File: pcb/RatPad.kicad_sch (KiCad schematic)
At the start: 26 parts, among them SW1 SW_Push, SW2 SW_Push, SW3 SW_Push, SW4 SW_Push, SW5 SW_Push, SW6 SW_Push, SW7 SW_Push, SW8 SW_Push, U1 XIAO-RP2040-DIP

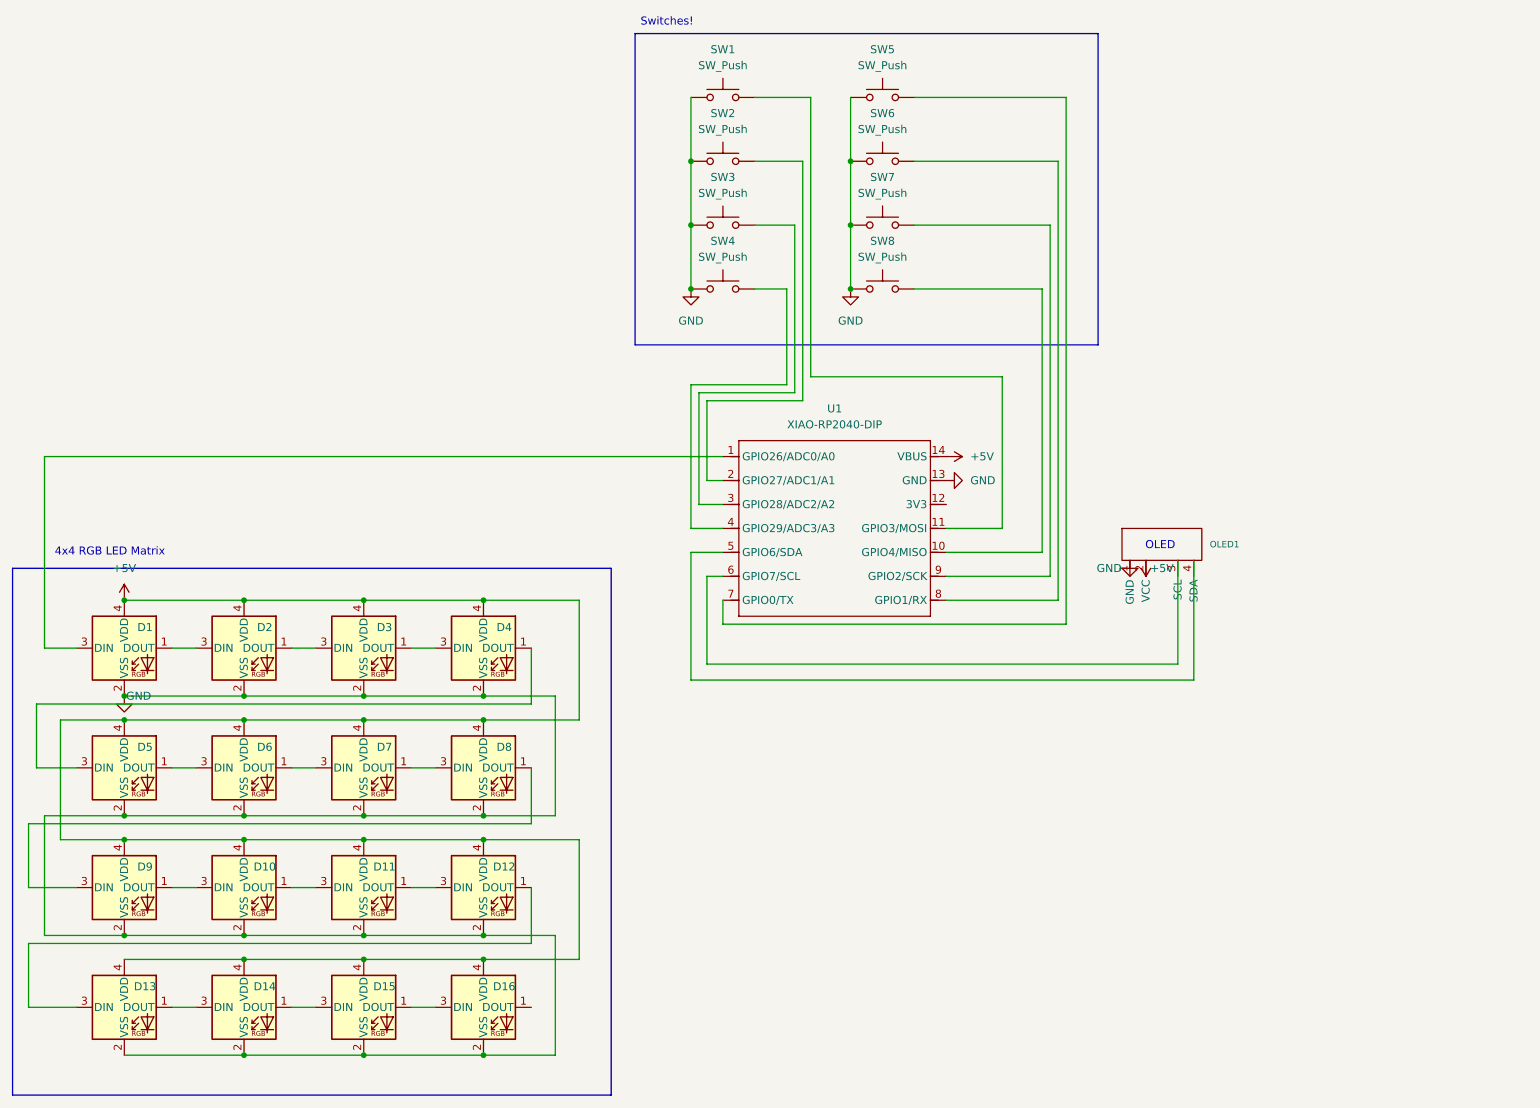
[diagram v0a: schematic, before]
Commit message: Add case and update PCB
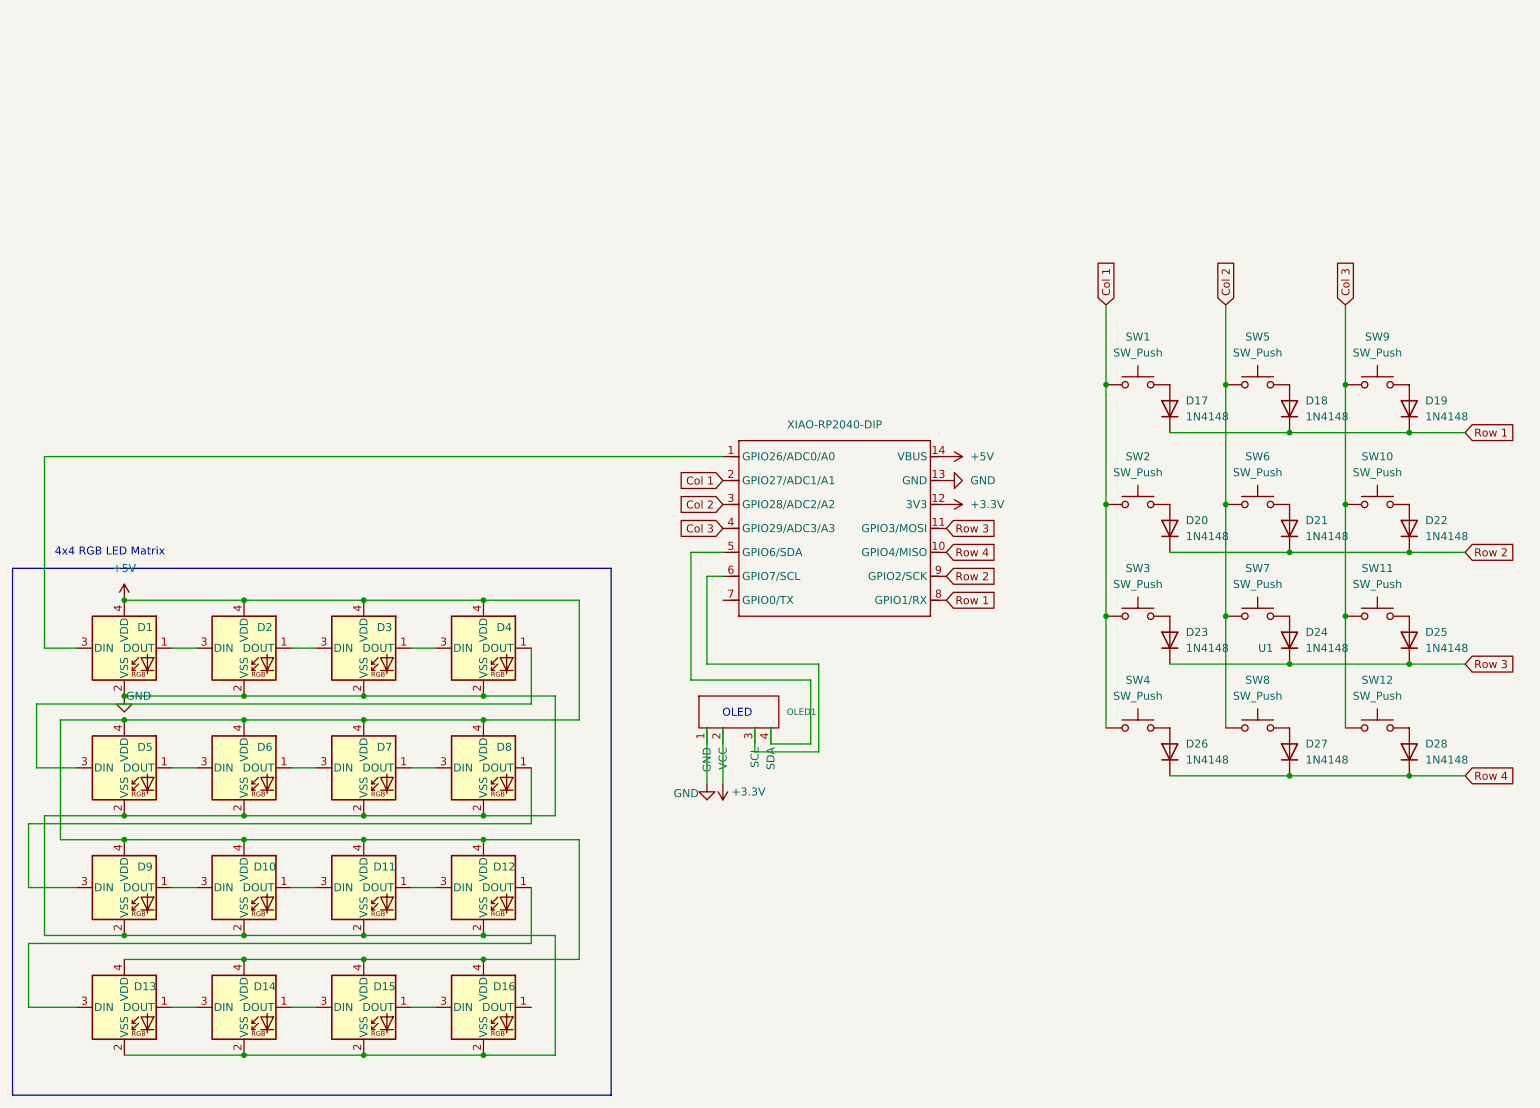
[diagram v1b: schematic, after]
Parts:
- added D17, D18, D19, D20, D21, D22, D23, D24, D25, D26, D27, D28: 1N4148, Diode_THT:D_DO-35_SOD27_P7.62mm_Horizontal, symbol Diode:1N4148
- added SW10, SW11, SW12, SW9: SW_Push, Button_Switch_Keyboard:SW_Cherry_MX_1.00u_PCB, symbol Switch:SW_Push
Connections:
- net +5V: no longer OLED1.2 (VCC)
- net GND: no longer SW1.1, SW2.1, SW3.1, SW4.1, SW5.1, SW6.1, SW7.1, SW8.1
- net at SW4.2: now also D26.2 (A); no longer U1.4 (GPIO29/ADC3/A3)
- net at SW5.2: now also D18.2 (A); no longer U1.7 (GPIO0/TX)
- net at SW7.2: now also D24.2 (A); no longer U1.9 (GPIO2/SCK)
- net at SW8.2: now also D27.2 (A); no longer U1.10 (GPIO4/MISO)
- net at SW1.2: now also D17.2 (A); no longer U1.11 (GPIO3/MOSI)
- net +3.3V: now reaches U1.12 (3V3)
- net +3.3V: now also OLED1.2 (VCC)
- net at SW2.2: now also D20.2 (A); no longer U1.2 (GPIO27/ADC1/A1)
- net at SW3.2: now also D23.2 (A); no longer U1.3 (GPIO28/ADC2/A2)
- net at SW6.2: now also D21.2 (A); no longer U1.8 (GPIO1/RX)
- new net: D22.2 (A), SW10.2
- new net: D28.2 (A), SW12.2
- new net: D19.2 (A), SW9.2
- new net: D25.2 (A), SW11.2
- new net Col 1: SW1.1, SW2.1, SW3.1, SW4.1, U1.2 (GPIO27/ADC1/A1)
- new net Col 2: SW5.1, SW6.1, SW7.1, SW8.1, U1.3 (GPIO28/ADC2/A2)
- new net Col 3: SW10.1, SW11.1, SW12.1, SW9.1, U1.4 (GPIO29/ADC3/A3)
- new net Row 1: D17.1 (K), D18.1 (K), D19.1 (K), U1.8 (GPIO1/RX)
- new net Row 2: D20.1 (K), D21.1 (K), D22.1 (K), U1.9 (GPIO2/SCK)
- new net Row 3: D23.1 (K), D24.1 (K), D25.1 (K), U1.11 (GPIO3/MOSI)
- new net Row 4: D26.1 (K), D27.1 (K), D28.1 (K), U1.10 (GPIO4/MISO)
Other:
- note removed: "Switches!"
- title: RatPad V1 -> RatPad V2
- moved on the sheet: OLED1
